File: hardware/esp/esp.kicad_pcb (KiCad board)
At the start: 2 copper layers, 100 x 80 mm, 82 parts, among them J1 USB_C_Receptacle_USB2.0_16P, J2 Conn_01x02, J3 USB_C_Receptacle_USB2.0_16P, J4 Conn_01x02, J5 Conn_01x06_Pin, J6 Conn_01x09_Pin, J7 Conn_01x09_Pin, SW1 RESET, SW2 BOOT, U1 AMS1117-3.3, U2 ESP32-S3-WROOM-1, U3 VL53L0X, U4 NRF24L01, U5 BME280, U6 CP2102N-Axx-xQFN20, Y1 16MHz

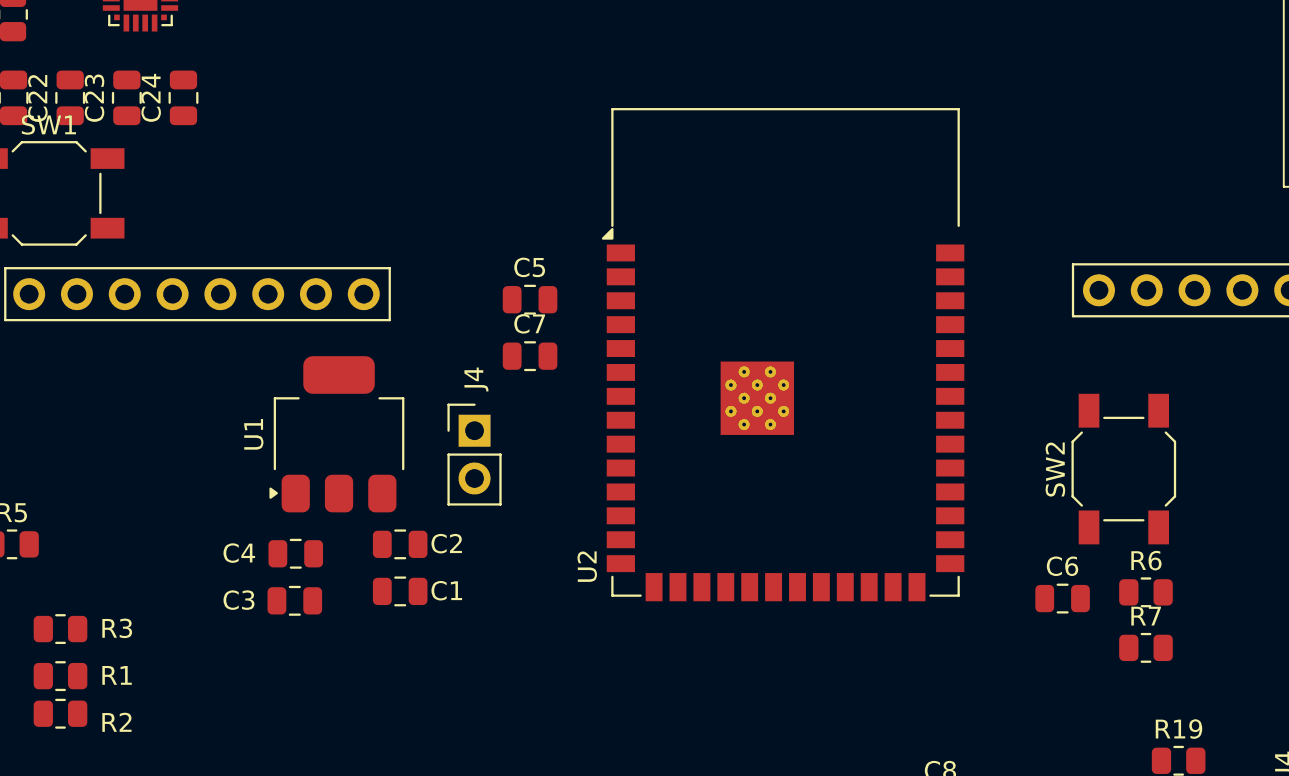
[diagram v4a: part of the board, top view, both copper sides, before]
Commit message: Removing UART LEDs
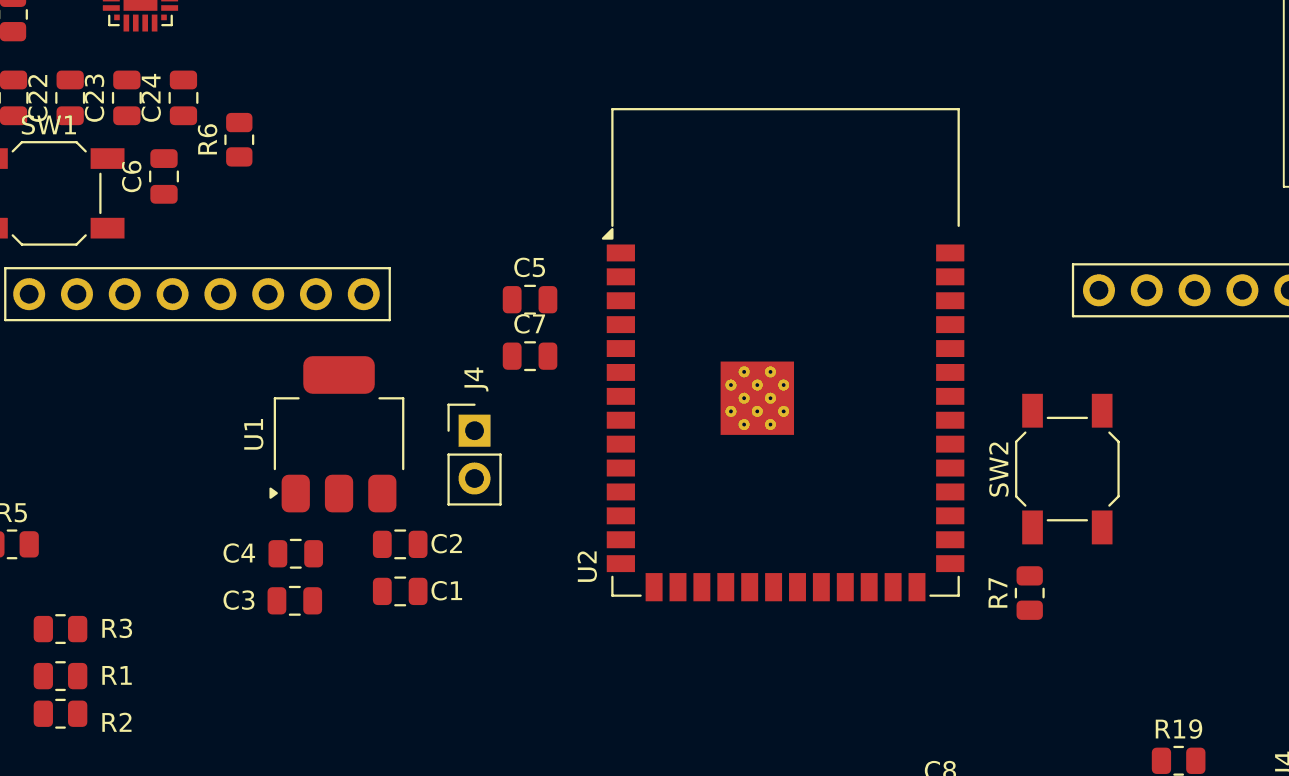
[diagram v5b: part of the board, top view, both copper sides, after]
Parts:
- moved R6 53.8 mm to (107.0, 96.5), turned to 90 degrees
- moved C6 52.8 mm to (103.0, 98.4), turned to 90 degrees
- moved R7 6.83 mm to (149.0, 120.6), turned to 90 degrees
- moved SW2 3.00 mm to (151.0, 114.0)

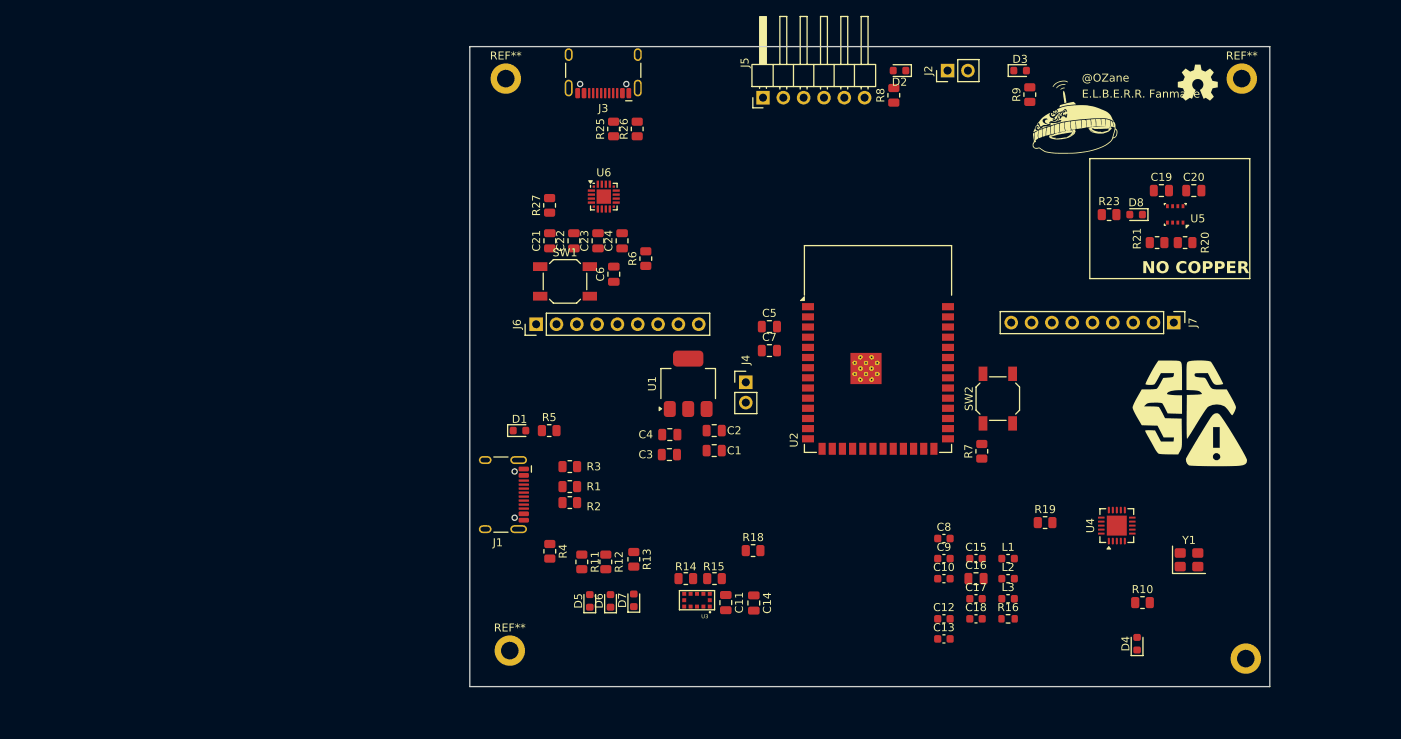
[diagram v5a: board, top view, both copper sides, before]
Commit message: Placing components on PCB and starting routing
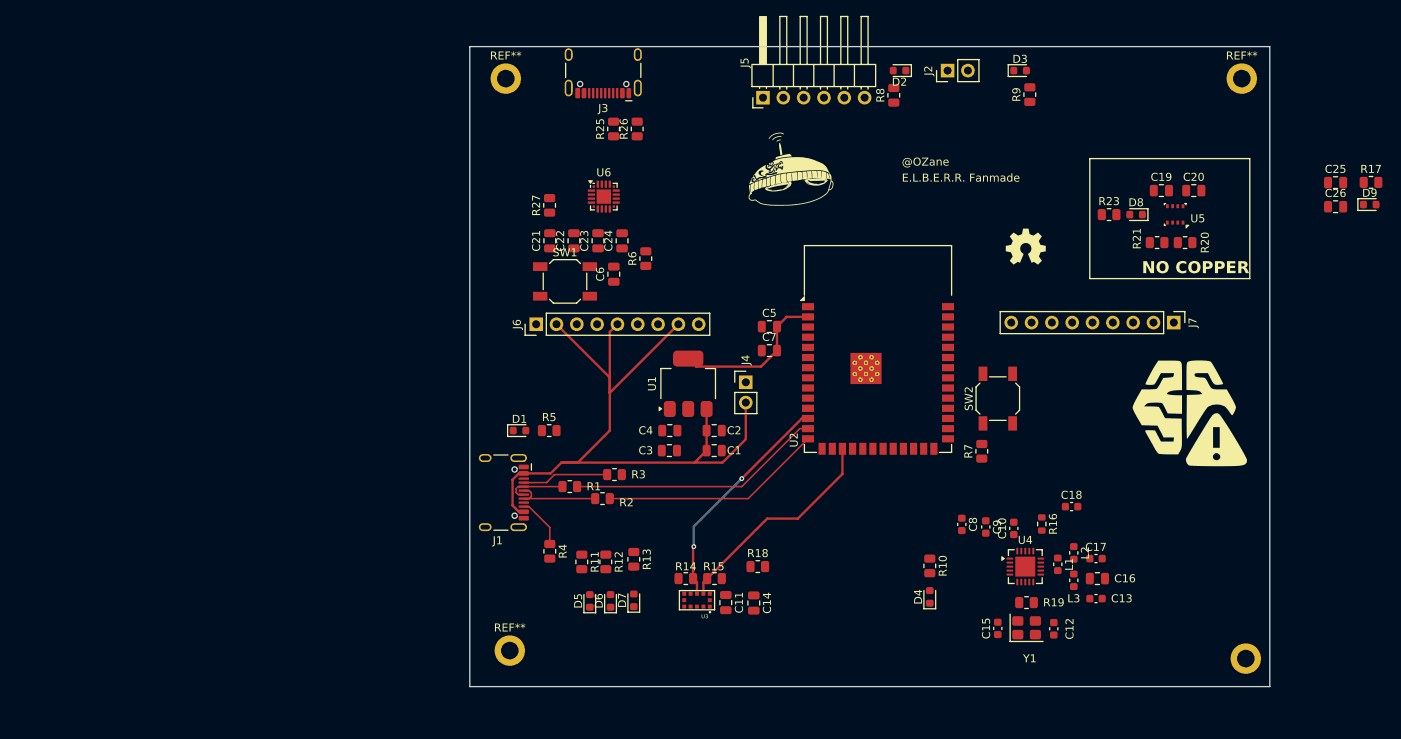
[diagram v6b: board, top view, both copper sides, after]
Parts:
- added C25: C, Capacitor_SMD:C_0805_2012Metric, F.Cu at (193.2, 87.0)
- added C26: C, Capacitor_SMD:C_0805_2012Metric, F.Cu at (193.2, 90.0)
- added D9: LED, LED_SMD:LED_0603_1608Metric, F.Cu at (197.5, 89.7)
- added R17: R, Resistor_SMD:R_0805_2012Metric, F.Cu at (197.7, 87.0)
- L3: value 2.7nH -> 3.9nH
- moved G*** 36.1 mm to (125.5, 87.5)
- moved G*** 29.7 mm to (154.5, 95.0)
- moved R10 27.0 mm to (142.5, 134.9), turned to -90 degrees
- moved D4 26.6 mm to (142.5, 138.8)
- moved Y1 22.0 mm to (154.6, 142.7)
- moved C13 19.7 mm to (163.3, 139.0)
- moved C18 18.4 mm to (160.2, 127.5)
- moved C17 15.8 mm to (163.3, 134.0)
- moved C16 15.2 mm to (163.4, 136.5)
- moved C12 13.8 mm to (158.0, 142.8), turned to 90 degrees
- moved R16 12.6 mm to (156.5, 129.7), turned to -90 degrees
- moved U4 12.5 mm to (154.4, 135.0), turned to 0 degrees
- moved C10 10.8 mm to (153.0, 130.2), turned to 90 degrees
- moved R19 10.3 mm to (154.6, 139.5), turned to 180 degrees
- moved C15 9.14 mm to (151.0, 142.7), turned to 90 degrees
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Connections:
- D2 pad 1: GND -> Net-(D2-K)
- R8 pad 1: RX_LED -> +3V3
- U2 pad 36: unconnected-(U2-RXD0-Pad36) -> TX
- U2 pad 37: unconnected-(U2-TXD0-Pad37) -> RX
- U2 pad 5: TX_LED -> unconnected-(U2-IO5-Pad5)
- U2 pad 6: RX_LED -> unconnected-(U2-IO6-Pad6)
- U6 pad 17: TX2 -> TX
- U6 pad 18: RX2 -> RX
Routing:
- net +5V: track 0.00 -> 93.0 mm
- net D-: track 0.00 -> 31.9 mm
- net SDA: track 0.00 -> 28.5 mm, vias 0 -> 2
- net D+: track 0.00 -> 27.9 mm
- net SCL: track 0.00 -> 27.6 mm
- net +3V3: track 0.00 -> 19.7 mm
- net Net-(J1-D+-PadA6): track 0.00 -> 11.5 mm
- net Net-(J1-CC1): track 0.00 -> 10.8 mm
- net Net-(J1-D--PadA7): track 0.00 -> 7.43 mm
- net Net-(J1-CC2): track 0.00 -> 6.40 mm

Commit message: Placing Bidirectional TVS diodes and fixing schematic + placing components on pcb
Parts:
- added D10: D_TVS, Diode_SMD:D_SOD-123, F.Cu at (97.5, 79.5)
- added D2: D_TVS, Diode_SMD:D_SOD-123, F.Cu at (97.2, 85.0)
- added D3: D_TVS, Diode_SMD:D_SOD-123, F.Cu at (102.8, 83.8)
- R27: value 1k -> 4.7k
- moved U6 4.03 mm to (105.8, 89.2)
- moved D5 3.00 mm to (100.0, 142.3)
- moved D6 3.00 mm to (102.6, 142.3)
- moved D7 3.00 mm to (105.5, 142.2)
- moved R11 3.00 mm to (99.0, 137.4)
- moved R12 3.00 mm to (102.0, 137.4)
- moved R13 3.00 mm to (105.5, 137.1)
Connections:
- C22 pad 2: GND -> unconnected-(C22-Pad2)

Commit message: Updating pins, and scehmatic
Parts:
- added J5: Conn_Coaxial, Connector_Coaxial:U.FL_Molex_MCRF_73412-0110_Vertical, F.Cu at (170.4, 133.5)
- renumbered C23 to C10, C24 to C11, C8 to C12, C9 to C13, C10 to C14, C11 to C15, C12 to C16, C13 to C17, C14 to C18, C15 to C19, C16 to C20, C17 to C21, C18 to C22, C19 to C23, C20 to C24, C22 to C5, C21 to C6, C5 to C7, C6 to C8, C7 to C9, D3 to D1, D10 to D3, D1 to D4, D4 to D5, D5 to D6, D6 to D7, D7 to D8, D8 to D9, J4 to J1, J1 to J2, J2 to J4, J5 to J7, J7 to J8, R25 to R1, R7 to R10, R10 to R11, R11 to R12, R12 to R13, R13 to R14, R14 to R15, R15 to R16, R16 to R17, R19 to R18, R23 to R19, R26 to R2, R1 to R3, R2 to R4, R3 to R5, R4 to R6, R5 to R7, R27 to R8, R6 to R9, U6 to U2, U2 to U3, U3 to U4, U4 to U5, U5 to U6
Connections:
- D9 pad 2: Net-(D8-A) (its old number) -> Net-(D9-A)
- R19 pad 2: Net-(D8-A) (its old number) -> Net-(D9-A)
